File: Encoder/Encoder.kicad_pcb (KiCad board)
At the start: 2 copper layers, 22.9 x 22.9 mm, 11 parts, among them J1 Conn_01x04, U1 AS5600

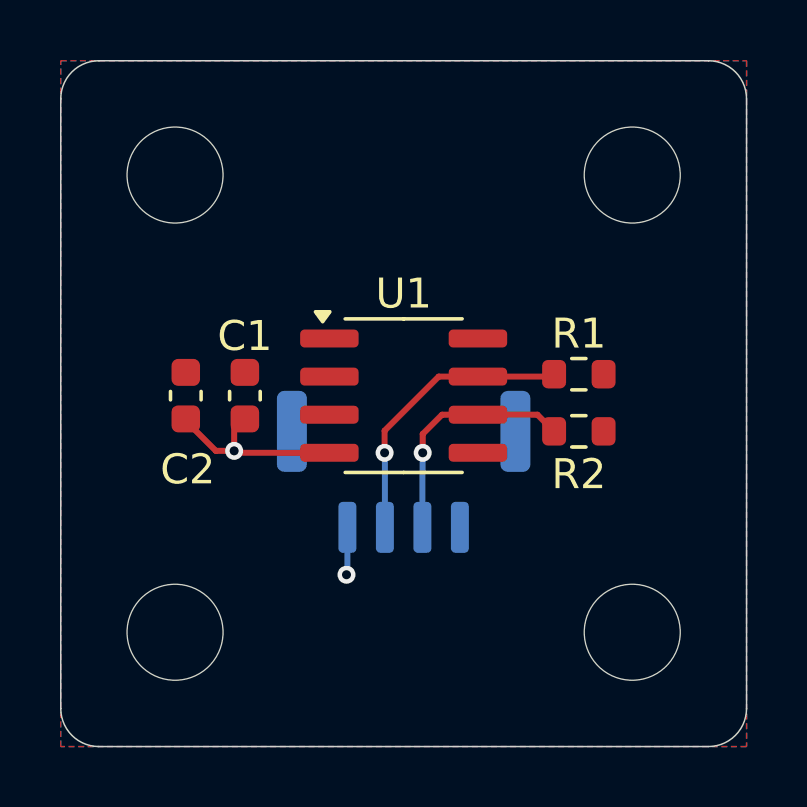
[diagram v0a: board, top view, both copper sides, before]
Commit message: Add switch for CW/CCW control
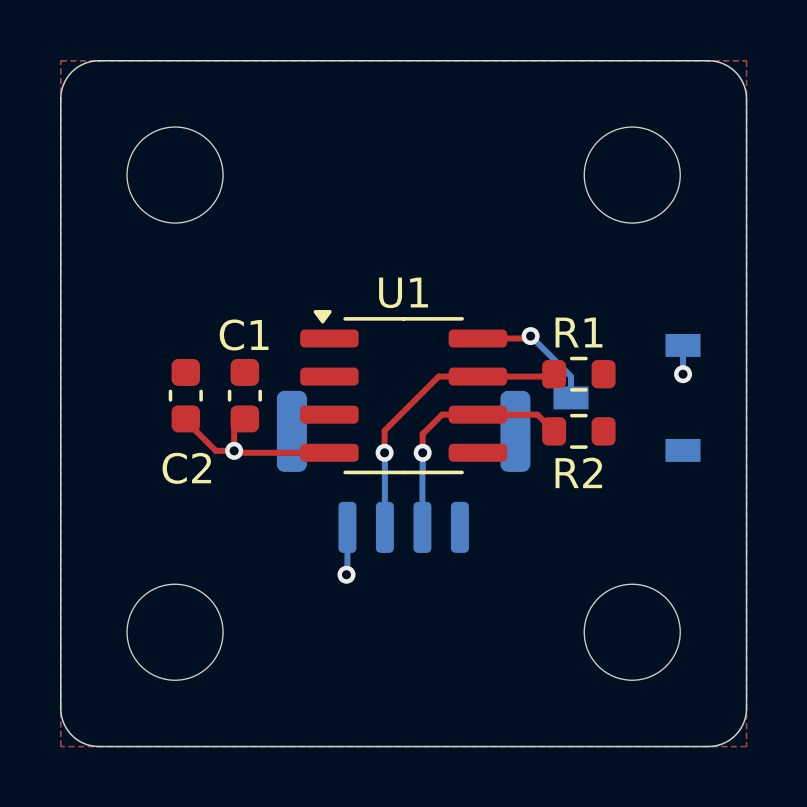
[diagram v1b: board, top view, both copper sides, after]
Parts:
- added SW1: CJS-1200TB, RoboMaster:CJS-1200B_NDC, B.Cu at (108.0, 62.4)
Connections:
- U1 pad 8: +3.3V -> /DIR
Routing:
- net /DIR: track 0.00 -> 4.41 mm, vias 0 -> 1
- net +3.3V: track 1.81 -> 2.77 mm, vias 1 -> 2
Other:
- board text added: "CCW"
- board text added: "CW"
